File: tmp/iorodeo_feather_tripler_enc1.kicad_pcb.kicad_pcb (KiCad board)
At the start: 2 copper layers, 105.7 x 69.6 mm, 14 parts, among them J1 Barrel_Jack_Switch, J2 Conn_01x04, J3 Conn_01x04, J4 Conn_01x04, J5 Conn_01x04, J6 Conn_01x04, M1 MountingHole_4.3mm_M4, M2 MountingHole_4.3mm_M4, M3 MountingHole_4.3mm_M4, M4 MountingHole_4.3mm_M4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

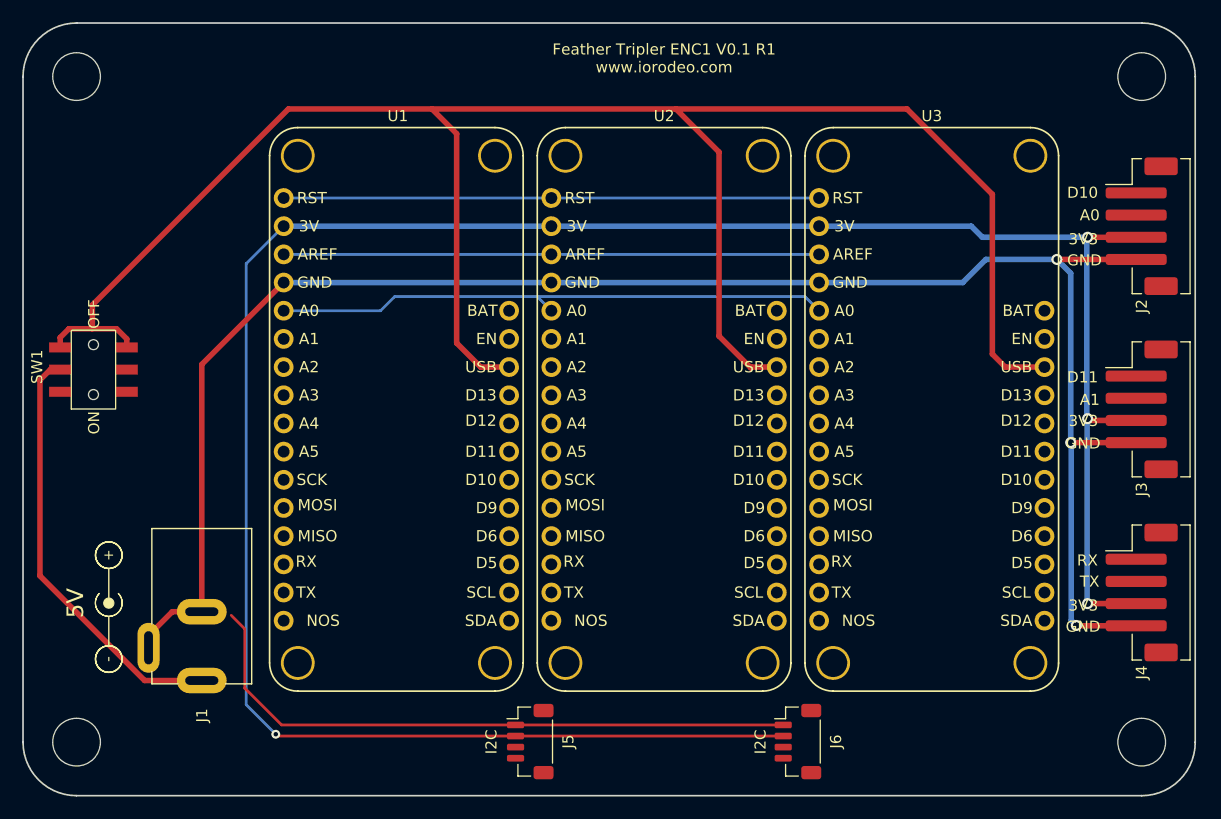
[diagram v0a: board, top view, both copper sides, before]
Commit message: Finished rerouting board.  Remade production files. Need to be checked.
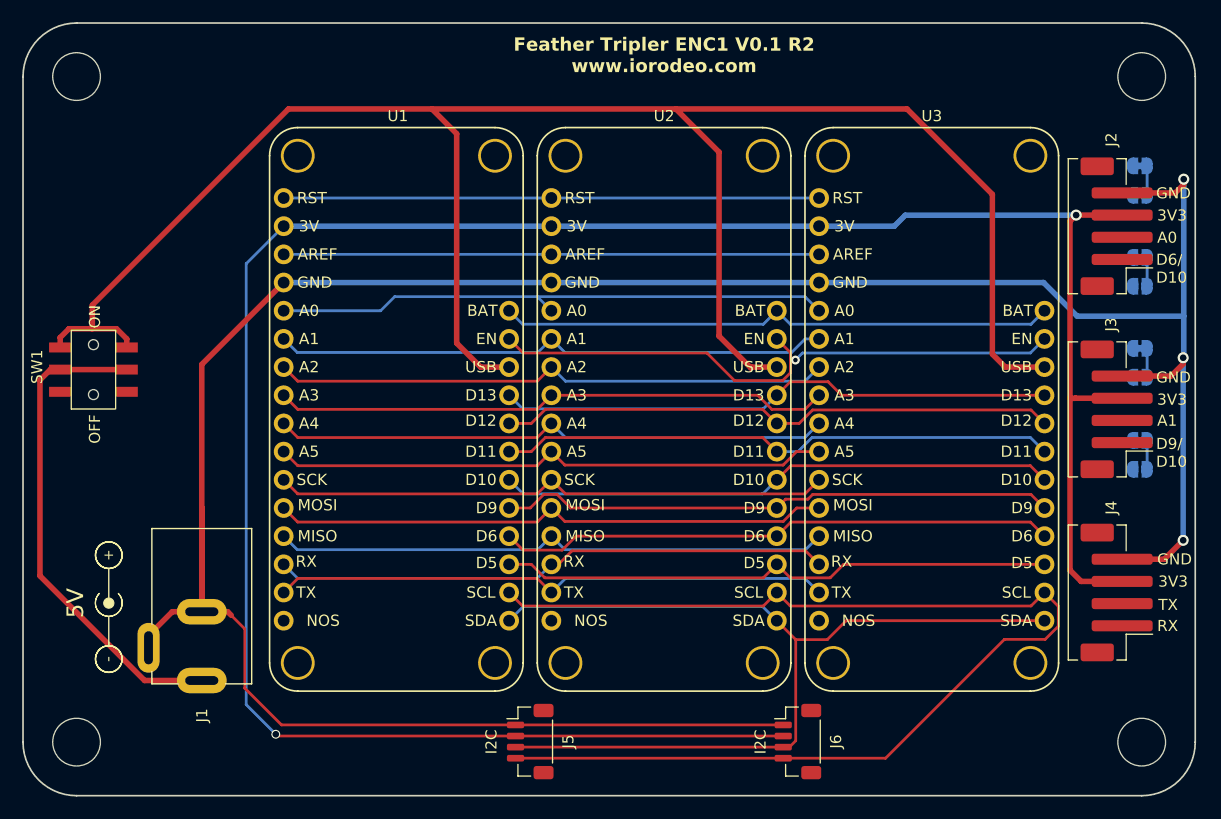
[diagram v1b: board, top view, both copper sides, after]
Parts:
- added JP1: SolderJumper_2_Bridged, Jumper:SolderJumper-2_P1.3mm_Bridged_RoundedPad1.0x1.5mm, B.Cu at (146.7, 67.1)
- added JP2: SolderJumper_2_Open, Jumper:SolderJumper-2_P1.3mm_Open_RoundedPad1.0x1.5mm, B.Cu at (146.7, 69.7)
- added JP3: SolderJumper_2_Bridged, Jumper:SolderJumper-2_P1.3mm_Bridged_RoundedPad1.0x1.5mm, B.Cu at (146.7, 58.9)
- added JP4: SolderJumper_2_Open, Jumper:SolderJumper-2_P1.3mm_Open_RoundedPad1.0x1.5mm, B.Cu at (146.7, 61.5)
- added JP5: SolderJumper_2_Bridged, Jumper:SolderJumper-2_P1.3mm_Bridged_RoundedPad1.0x1.5mm, B.Cu at (146.7, 83.6)
- added JP6: SolderJumper_2_Open, Jumper:SolderJumper-2_P1.3mm_Open_RoundedPad1.0x1.5mm, B.Cu at (146.7, 86.2)
- added JP7: SolderJumper_2_Bridged, Jumper:SolderJumper-2_P1.3mm_Bridged_RoundedPad1.0x1.5mm, B.Cu at (146.7, 75.3)
- added JP8: SolderJumper_2_Open, Jumper:SolderJumper-2_P1.3mm_Open_RoundedPad1.0x1.5mm, B.Cu at (146.7, 77.9)
- J2, J3, J4: footprint Connector_JST:JST_PH_B4B-PH-SM4-TB_1x04-1MP_P2.00mm_Vertical -> JST_PH_4Pin_Vertical:JST_PH_B4B-PH-SM4-TB_1x04-1MP_P2.00mm_Vertical
- moved J2 2.81 mm to (144.0, 64.3)
- moved J3 2.81 mm to (144.0, 80.8)
- moved J4 2.81 mm to (144.0, 97.3)
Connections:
- J2 pad 1: /D10 -> Net-(J2-Pin_1)
- J2 pad 2: /A0 -> Net-(J2-Pin_2)
- J3 pad 1: /D11 -> Net-(J3-Pin_1)
- J3 pad 2: /A1 -> Net-(J3-Pin_2)
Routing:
- net /SCL: track 0.00 -> 107.7 mm
- net /SDA: track 0.00 -> 85.3 mm
- net /EN: track 0.00 -> 54.5 mm, vias 0 -> 1
- net /D11: track 0.00 -> 50.4 mm
- net /A2: track 0.00 -> 50.4 mm
- net /D10: track 0.00 -> 50.4 mm
- net /SCK: track 0.00 -> 50.4 mm
- net /TX: track 0.00 -> 50.4 mm
- net /A4: track 0.00 -> 50.4 mm
- net /A3: track 0.00 -> 50.4 mm
- net /D6: track 0.00 -> 50.4 mm
- net /RX: track 0.00 -> 50.3 mm
- net /MOSI: track 0.00 -> 50.3 mm
- net /A5: track 0.00 -> 50.3 mm
- net /D12: track 0.00 -> 50.3 mm
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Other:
- board text added: "A2"
- board text added: "A3"
- board text added: "D6"
- board text added: "D6/ D10"
- board text added: "D9/ D10"
- board text added: "Feather Tripler ENC1 V0.1 R2 www.iorodeo.com"
- board text added: "J2 Pin1 Select"
- board text added: "J2 Pin2 Select"
- board text added: "J3 Pin1 Select"
- board text added: "J3 Pin2 Select"
- board text removed: "D11"
- board text removed: "Feather Tripler ENC1 V0.1 R1 www.iorodeo.com"
